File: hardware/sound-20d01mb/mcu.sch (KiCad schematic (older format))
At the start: 0 parts

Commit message: Added STM32F446RCTx
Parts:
- added U?: STM32F446RCTx, Package_QFP:LQFP-64_10x10mm_P0.5mm, symbol sound-20d01_Library:STM32F446RCTx
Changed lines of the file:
@@
 Comment4 ""
 $EndDescr
+$Comp
+L sound-20d01_Library:STM32F446RCTx U?
+U 1 1 60E3A9D6
+P 5300 3650
+F 0 "U?" H 5300 3700 50  0000 C CNN
+F 1 "STM32F446RCTx" H 5300 3600 50  0000 C CNN
+F 2 "Package_QFP:LQFP-64_10x10mm_P0.5mm" H 5300 2150 50  0001 C CNN
+F 3 "https://www.st.com/resource/en/datasheet/stm32f446rc.pdf" H 5300 2050 50  0001 C CNN
+	1    5300 3650
+	1    0    0    -1
+$EndComp
 $EndSCHEMATC

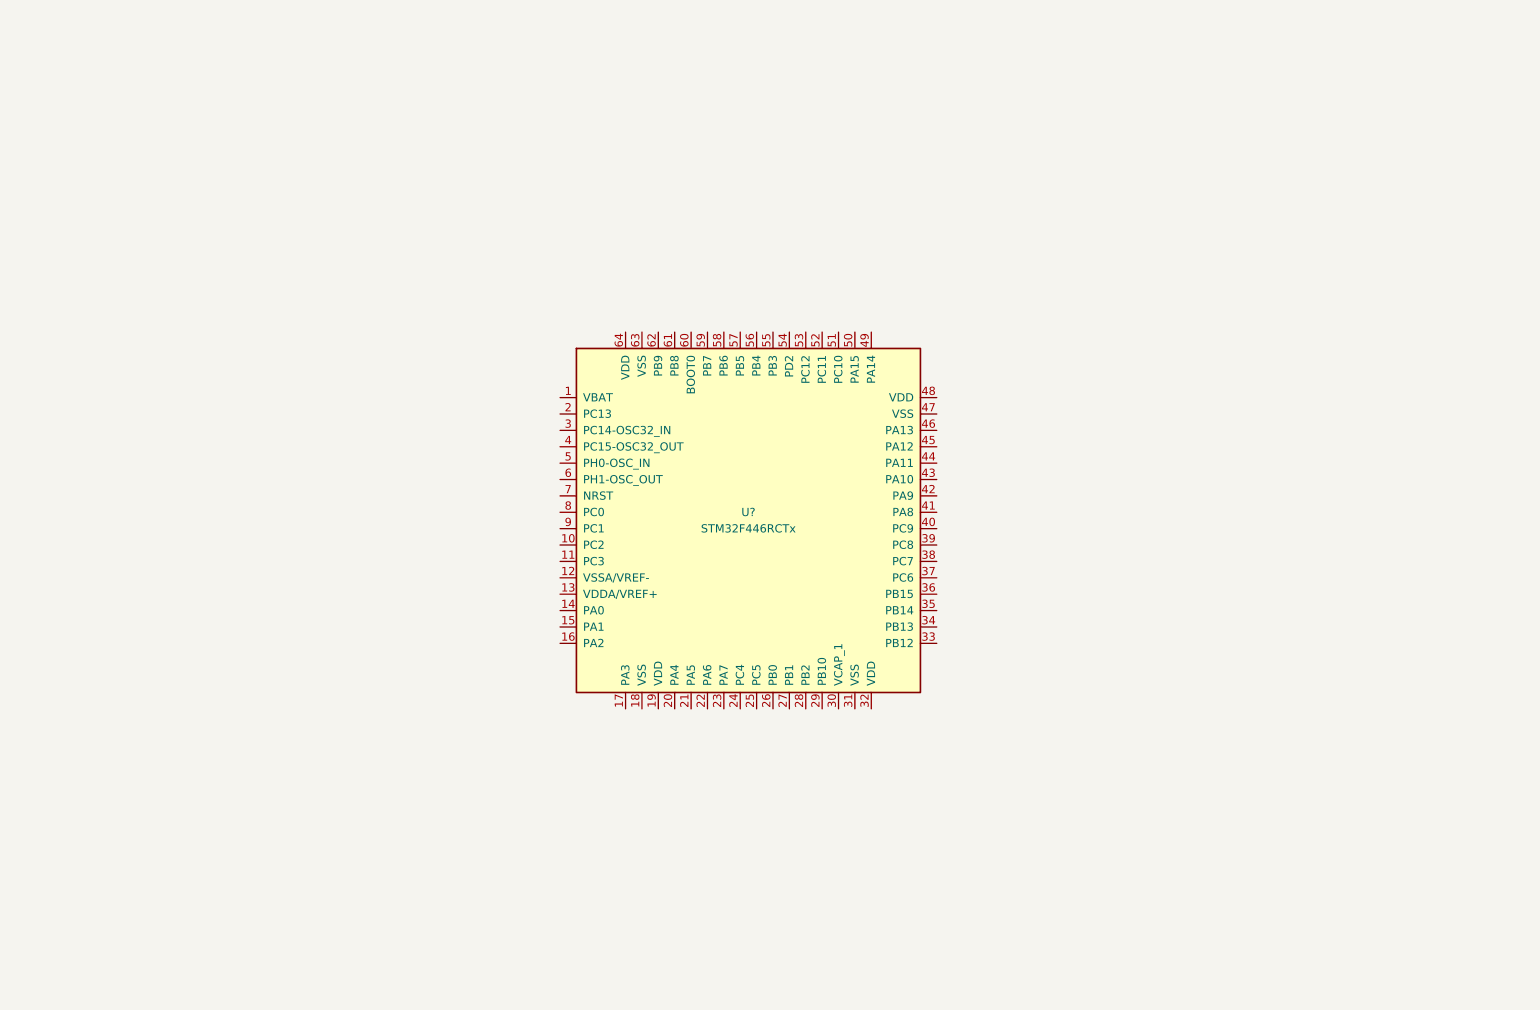
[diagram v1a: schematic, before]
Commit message: Updated MCU schematic
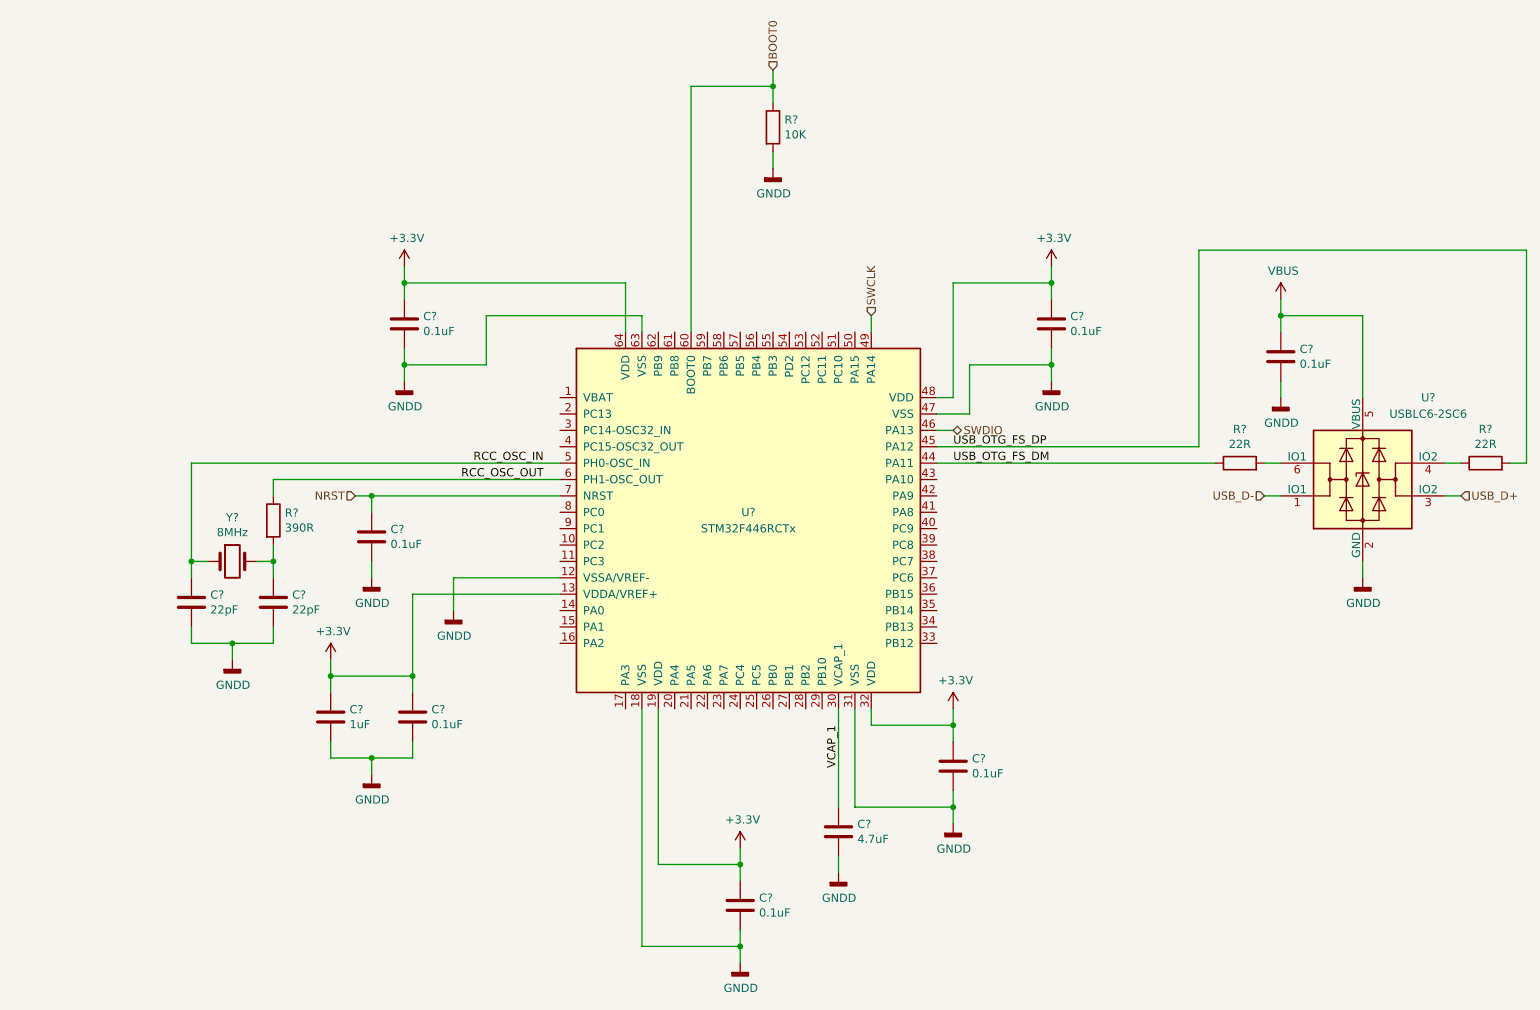
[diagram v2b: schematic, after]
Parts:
- added C?: 4.7uF, Capacitor_SMD:C_1206_3216Metric_Pad1.42x1.75mm_HandSolder, symbol Device:C
- added C? (x7): 0.1uF, Capacitor_SMD:C_1206_3216Metric_Pad1.42x1.75mm_HandSolder, symbol Device:C
- added C?: 1uF, Capacitor_SMD:C_1206_3216Metric_Pad1.42x1.75mm_HandSolder, symbol Device:C
- added C? (x2): 22pF, Capacitor_SMD:C_1206_3216Metric_Pad1.42x1.75mm_HandSolder, symbol Device:C
- added R? (x2): 22R, Resistor_SMD:R_1206_3216Metric_Pad1.42x1.75mm_HandSolder, symbol Device:R
- added R?: 10K, Resistor_SMD:R_1206_3216Metric_Pad1.42x1.75mm_HandSolder, symbol Device:R
- added R?: 390R, Resistor_SMD:R_1206_3216Metric_Pad1.42x1.75mm_HandSolder, symbol Device:R
- added U?: USBLC6-2SC6, Package_TO_SOT_SMD:SOT-23-6, symbol Power_Protection:USBLC6-2SC6
- added Y?: 8MHz, Crystal:Crystal_SMD_HC49-SD, symbol Device:Crystal
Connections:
- net GNDD: now reaches U?.12 (VSSA/VREF-)
- net GNDD: now also U?.18 (VSS), U?.31 (VSS), U?.47 (VSS), U?.63 (VSS), C?.2, C?.2, C?.2, C?.2, C?.2, C?.2, C?.2, C?.2, C?.2, C?.2, C?.2, R?.2, U?.2 (GND)
- net +3V3: now reaches U?.13 (VDDA/VREF+)
- net +3V3: now also U?.19 (VDD), U?.32 (VDD), U?.48 (VDD), U?.64 (VDD), C?.1, C?.1, C?.1, C?.1, C?.1, C?.1
- net VCAP_1: now reaches U?.30 (VCAP_1)
- net VCAP_1: now also C?.1
- net USB_OTG_FS_DM: now reaches U?.44 (PA11)
- net USB_OTG_FS_DM: now also R?.1
- net USB_OTG_FS_DP: now reaches U?.45 (PA12)
- net USB_OTG_FS_DP: now also R?.2
- net SWDIO: now reaches U?.46 (PA13)
- net SWCLK: now reaches U?.49 (PA14)
- net RCC_OSC_IN: now reaches U?.5 (PH0-OSC_IN)
- net RCC_OSC_IN: now also C?.1, Y?.1
- net RCC_OSC_OUT: now reaches U?.6 (PH1-OSC_OUT)
- net RCC_OSC_OUT: now also R?.1
- net BOOT0: now reaches U?.60 (BOOT0)
- net BOOT0: now also R?.1
- net NRST: now reaches U?.7 (NRST)
- net NRST: now also C?.1
- new net: R?.1, U?.4 (IO2)
- new net: R?.2, U?.6 (IO1)
- new net: C?.1, R?.2, Y?.2
- new net USB_D+: U?.3 (IO2)
- new net USB_D-: U?.1 (IO1)
- new net VBUS: C?.1, U?.5 (VBUS)

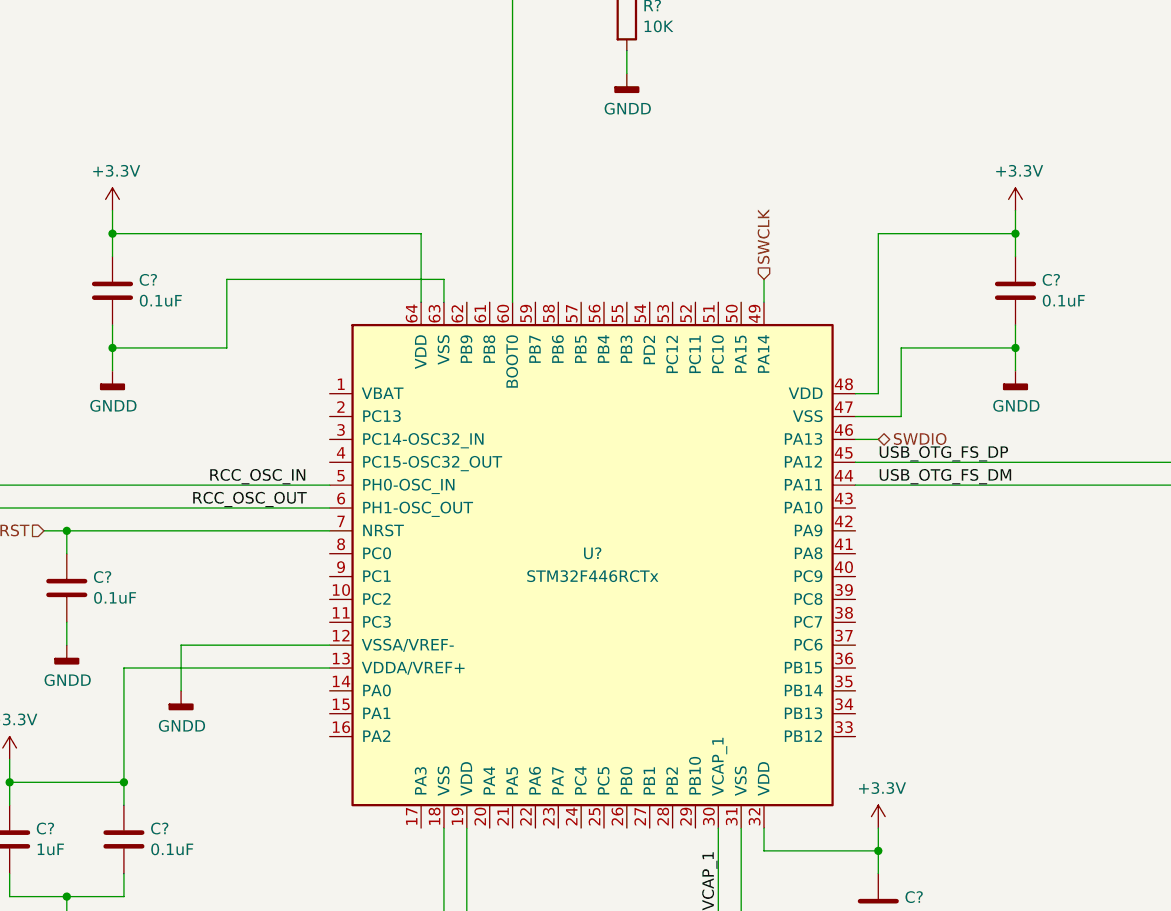
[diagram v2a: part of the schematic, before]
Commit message: Connected MCU to DAC
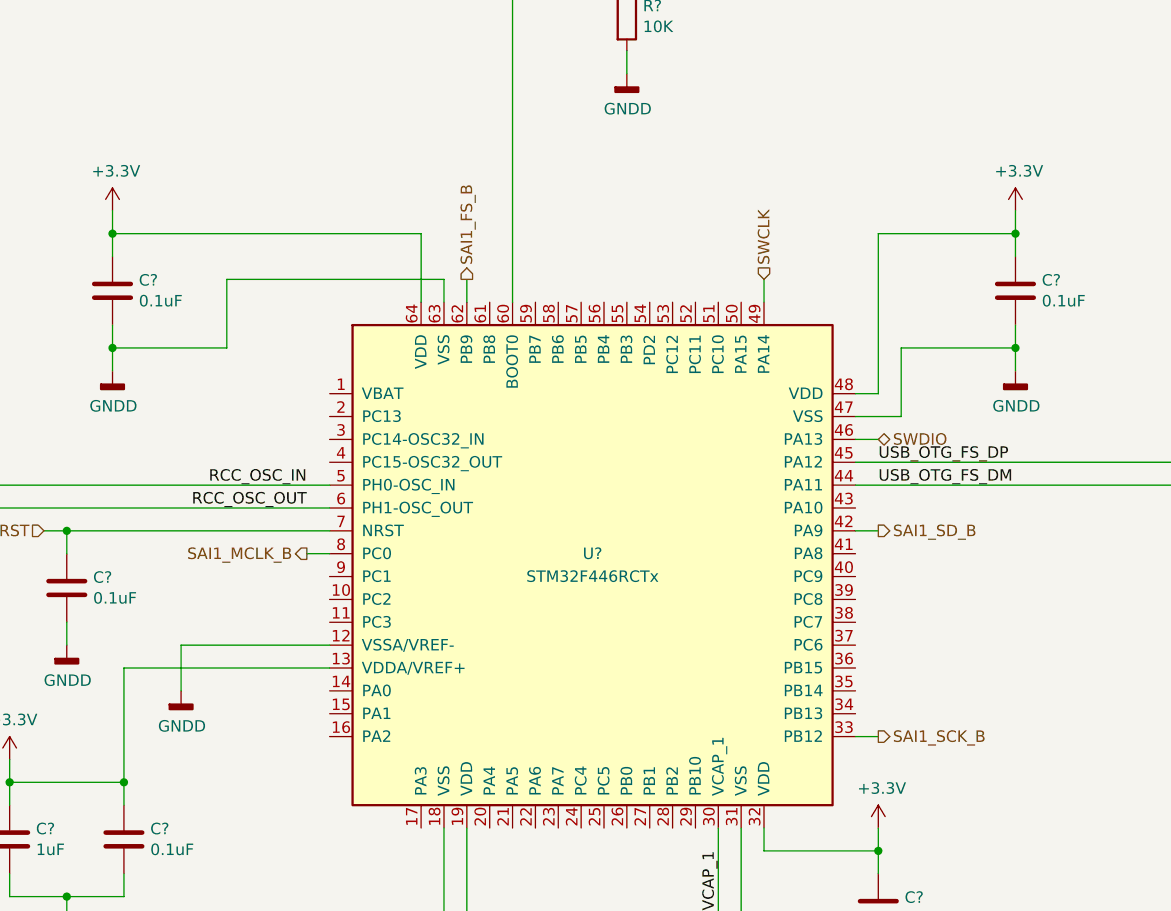
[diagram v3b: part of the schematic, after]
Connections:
- net SAI1_SCK_B: now reaches U?.33 (PB12)
- net SAI1_SD_B: now reaches U?.42 (PA9)
- net SAI1_FS_B: now reaches U?.62 (PB9)
- net SAI1_MCLK_B: now reaches U?.8 (PC0)
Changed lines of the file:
@@
 Wire Wire Line
 	5850 4800 5850 5400
+Text HLabel 4750 2400 1    50   Output ~ 0
+SAI1_FS_B
+Wire Wire Line
+	4750 2500 4750 2400
+Text HLabel 6550 3500 2    50   Output ~ 0
+SAI1_SD_B
+Wire Wire Line
+	6450 3500 6550 3500
+Text HLabel 6550 4400 2    50   Output ~ 0
+SAI1_SCK_B
+Wire Wire Line
+	6450 4400 6550 4400
+Text HLabel 4050 3600 0    50   Output ~ 0
+SAI1_MCLK_B
+Wire Wire Line
+	4150 3600 4050 3600
 $EndSCHEMATC

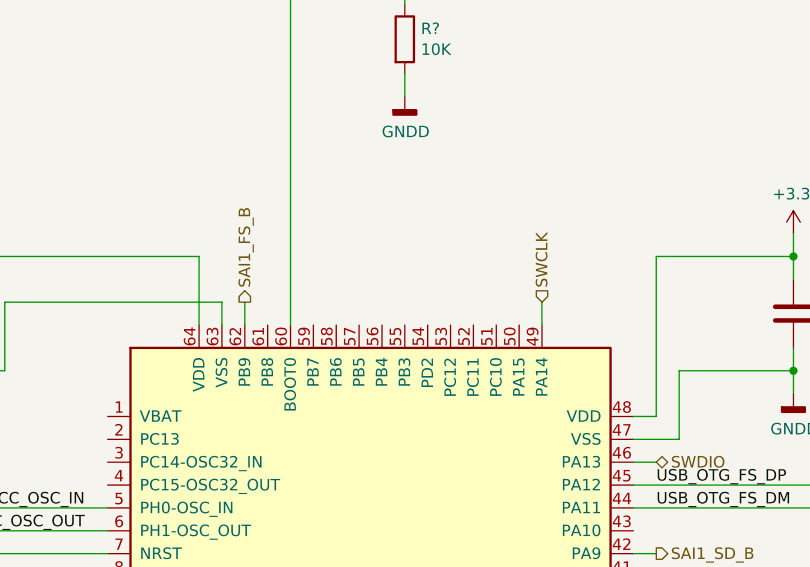
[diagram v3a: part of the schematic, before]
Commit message: Added SWO
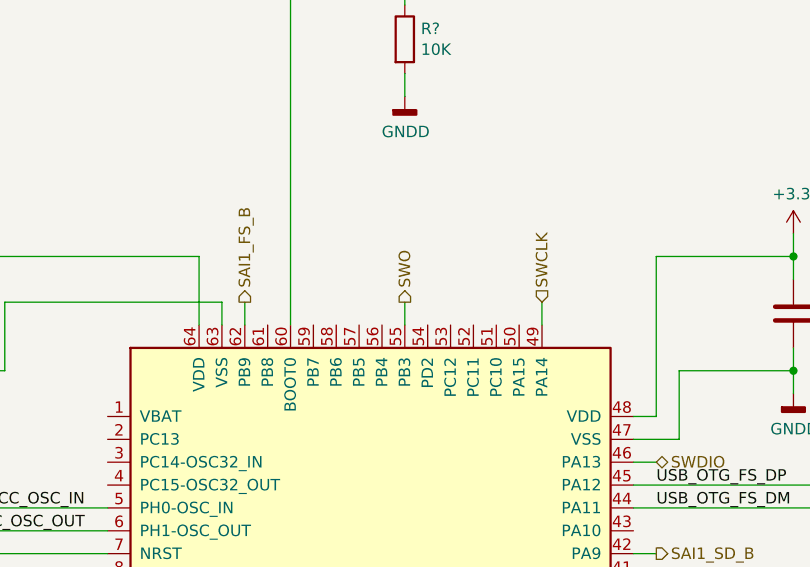
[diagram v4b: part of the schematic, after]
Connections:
- net SWO: now reaches U?.55 (PB3)
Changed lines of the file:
@@
 Wire Wire Line
 	4150 3600 4050 3600
+Text HLabel 5450 2400 1    50   Output ~ 0
+SWO
+Wire Wire Line
+	5450 2500 5450 2400
 $EndSCHEMATC

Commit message: Added OSC32
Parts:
- added C? (x2): C, Capacitor_SMD:C_1206_3216Metric_Pad1.42x1.75mm_HandSolder, symbol Device:C
- added Y?: 32.768kHz, Crystal:Crystal_SMD_3215-2Pin_3.2x1.5mm, symbol Device:Crystal
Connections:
- net GNDD: now also C?.2, C?.2
- net RCC_OSC32_IN: now reaches U?.3 (PC14-OSC32_IN)
- net RCC_OSC32_IN: now also C?.1, Y?.1
- net RCC_OSC32_OUT: now reaches U?.4 (PC15-OSC32_OUT)
- net RCC_OSC32_OUT: now also C?.1, Y?.2
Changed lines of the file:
@@
 Wire Wire Line
 	5450 2500 5450 2400
+$Comp
+L Device:Crystal Y?
+U 1 1 60E3EBB3
+P 1150 3900
+F 0 "Y?" H 1150 4168 50  0000 C CNN
+F 1 "32.768kHz" H 1150 4077 50  0000 C CNN
+F 2 "Crystal:Crystal_SMD_3215-2Pin_3.2x1.5mm" H 1150 3900 50  0001 C CNN
+F 3 "~" H 1150 3900 50  0001 C CNN
+	1    1150 3900
+	1    0    0    -1
+$EndComp
+$Comp
+L power:GNDD #PWR?
+U 1 1 60E3ED93
+P 1150 4500
+F 0 "#PWR?" H 1150 4250 50  0001 C CNN
+F 1 "GNDD" H 1154 4345 50  0000 C CNN
+F 2 "" H 1150 4500 50  0001 C CNN
+F 3 "" H 1150 4500 50  0001 C CNN
+	1    1150 4500
+	1    0    0    -1
+$EndComp
+Wire Wire Line
+	900  4300 900  4400
+Wire Wire Line
+	900  4400 1150 4400
+Wire Wire Line
+	1150 4400 1150 4500
+Wire Wire Line
+	1400 4300 1400 4400
+Wire Wire Line
+	1400 4400 1150 4400
+Connection ~ 1150 4400
+Wire Wire Line
+	4150 3200 1400 3200
+Wire Wire Line
+	1400 3200 1400 3900
+Wire Wire Line
+	1400 3900 1300 3900
+Wire Wire Line
+	1400 3900 1400 4000
+Connection ~ 1400 3900
+Wire Wire Line
+	4150 3100 900  3100
+Wire Wire Line
+	900  3100 900  3900
+Wire Wire Line
+	900  3900 1000 3900
+Wire Wire Line
+	900  3900 900  4000
+Connection ~ 900  3900
+Text Label 4050 3100 2    50   ~ 0
+RCC_OSC32_IN
+Text Label 4050 3200 2    50   ~ 0
+RCC_OSC32_OUT
+$Comp
+L Device:C C?
+U 1 1 60E6BE1E
+P 900 4150
+F 0 "C?" H 1015 4196 50  0000 L CNN
+F 1 "C" H 1015 4105 50  0000 L CNN
+F 2 "Capacitor_SMD:C_1206_3216Metric_Pad1.42x1.75mm_HandSolder" H 938 4000 50  0001 C CNN
+F 3 "~" H 900 4150 50  0001 C CNN
+	1    900  4150
+	1    0    0    -1
+$EndComp
+$Comp
+L Device:C C?
+U 1 1 60E6F7A2
+P 1400 4150
+F 0 "C?" H 1515 4196 50  0000 L CNN
+F 1 "C" H 1515 4105 50  0000 L CNN
+F 2 "Capacitor_SMD:C_1206_3216Metric_Pad1.42x1.75mm_HandSolder" H 1438 4000 50  0001 C CNN
+F 3 "~" H 1400 4150 50  0001 C CNN
+	1    1400 4150
+	1    0    0    -1
+$EndComp
 $EndSCHEMATC

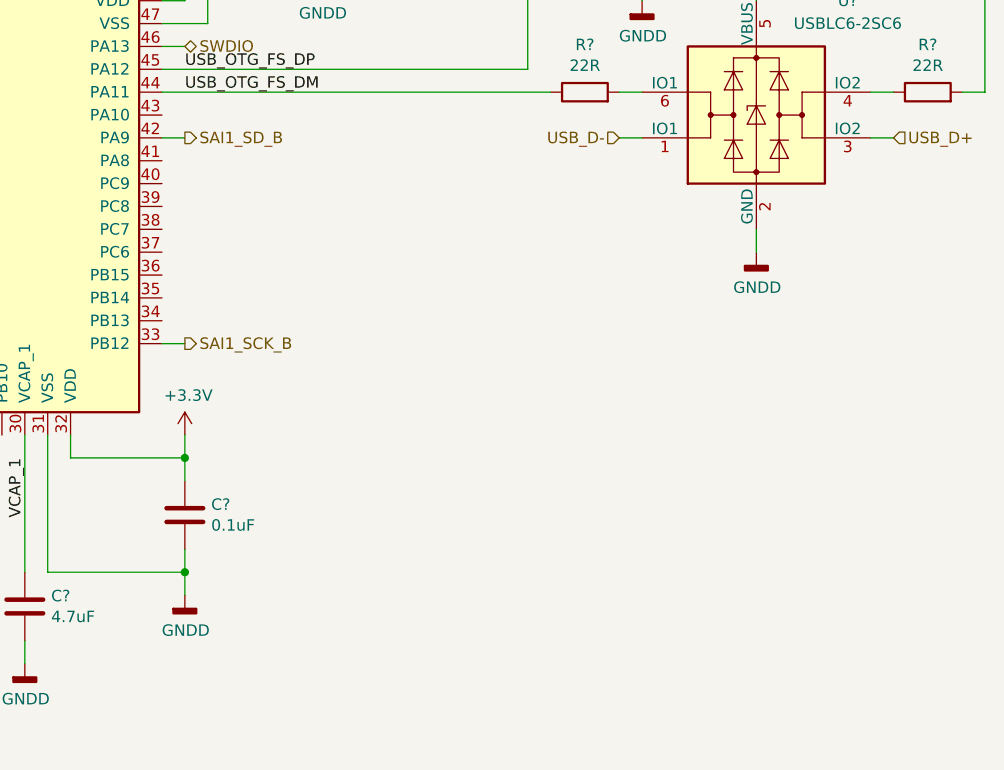
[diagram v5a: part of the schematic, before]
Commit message: Added oscillators sheet
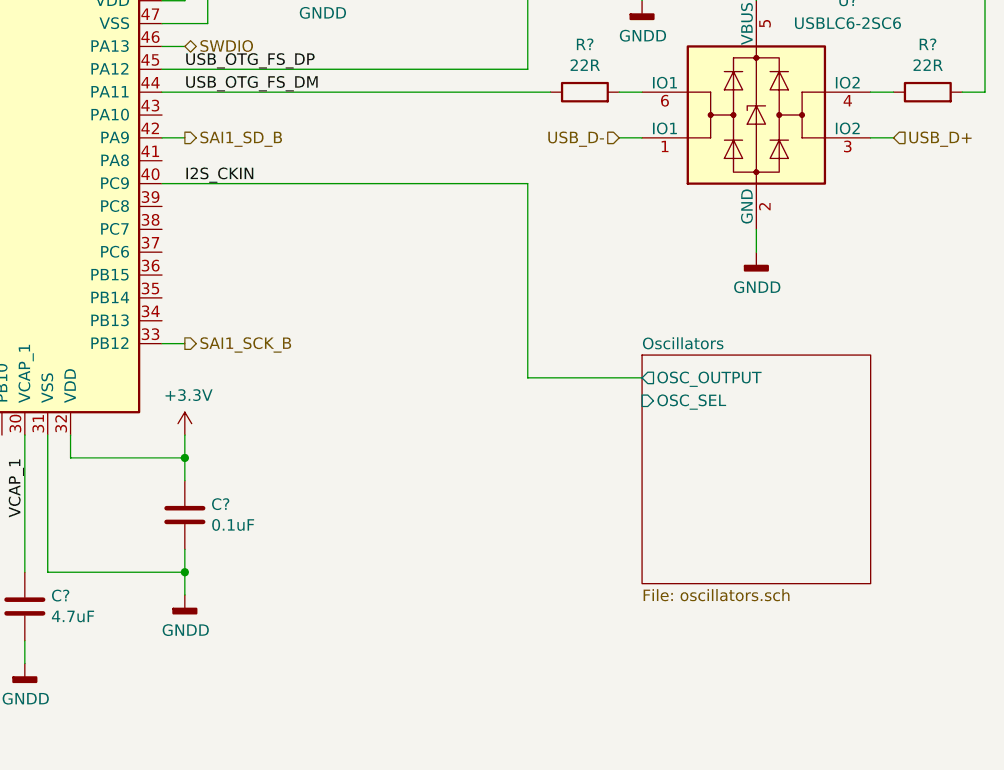
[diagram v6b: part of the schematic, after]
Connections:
- net I2S_CKIN: now reaches U?.40 (PC9)
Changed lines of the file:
@@
 $Descr A4 11693 8268
 encoding utf-8
-Sheet 2 5
+Sheet 2 6
 Title "Sound-20D01MB"
 Date "2021-07-01"
@@
 	1    0    0    -1
 $EndComp
+$Sheet
+S 8550 4450 1000 1000
+U 612AF97F
+F0 "Oscillators" 50
+F1 "oscillators.sch" 50
+F2 "OSC_OUTPUT" O L 8550 4550 50
+F3 "OSC_SEL" I L 8550 4650 50
+$EndSheet
+Wire Wire Line
+	8550 4550 8050 4550
+Wire Wire Line
+	8050 4550 8050 3700
+Wire Wire Line
+	8050 3700 6450 3700
+Text Label 6550 3700 0    50   ~ 0
+I2S_CKIN
 $EndSCHEMATC

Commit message: Added OSC
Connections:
- net OSC_SEL: now reaches U?.10 (PC2)
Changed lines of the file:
@@
 Text Label 6550 3700 0    50   ~ 0
 I2S_CKIN
+Text GLabel 4050 3800 0    50   Output ~ 0
+OSC_SEL
+Wire Wire Line
+	4150 3800 4050 3800
+Text GLabel 8450 4650 0    50   Input ~ 0
+OSC_SEL
+Wire Wire Line
+	8450 4650 8550 4650
 $EndSCHEMATC
